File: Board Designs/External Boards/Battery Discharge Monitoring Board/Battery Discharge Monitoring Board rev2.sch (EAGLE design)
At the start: 76 parts, among them Q1 LMMBT3904LT3G, Q2 LMMBT3904LT3G, Q3 LMMBT3904LT3G, Q4 LMMBT3904LT3G

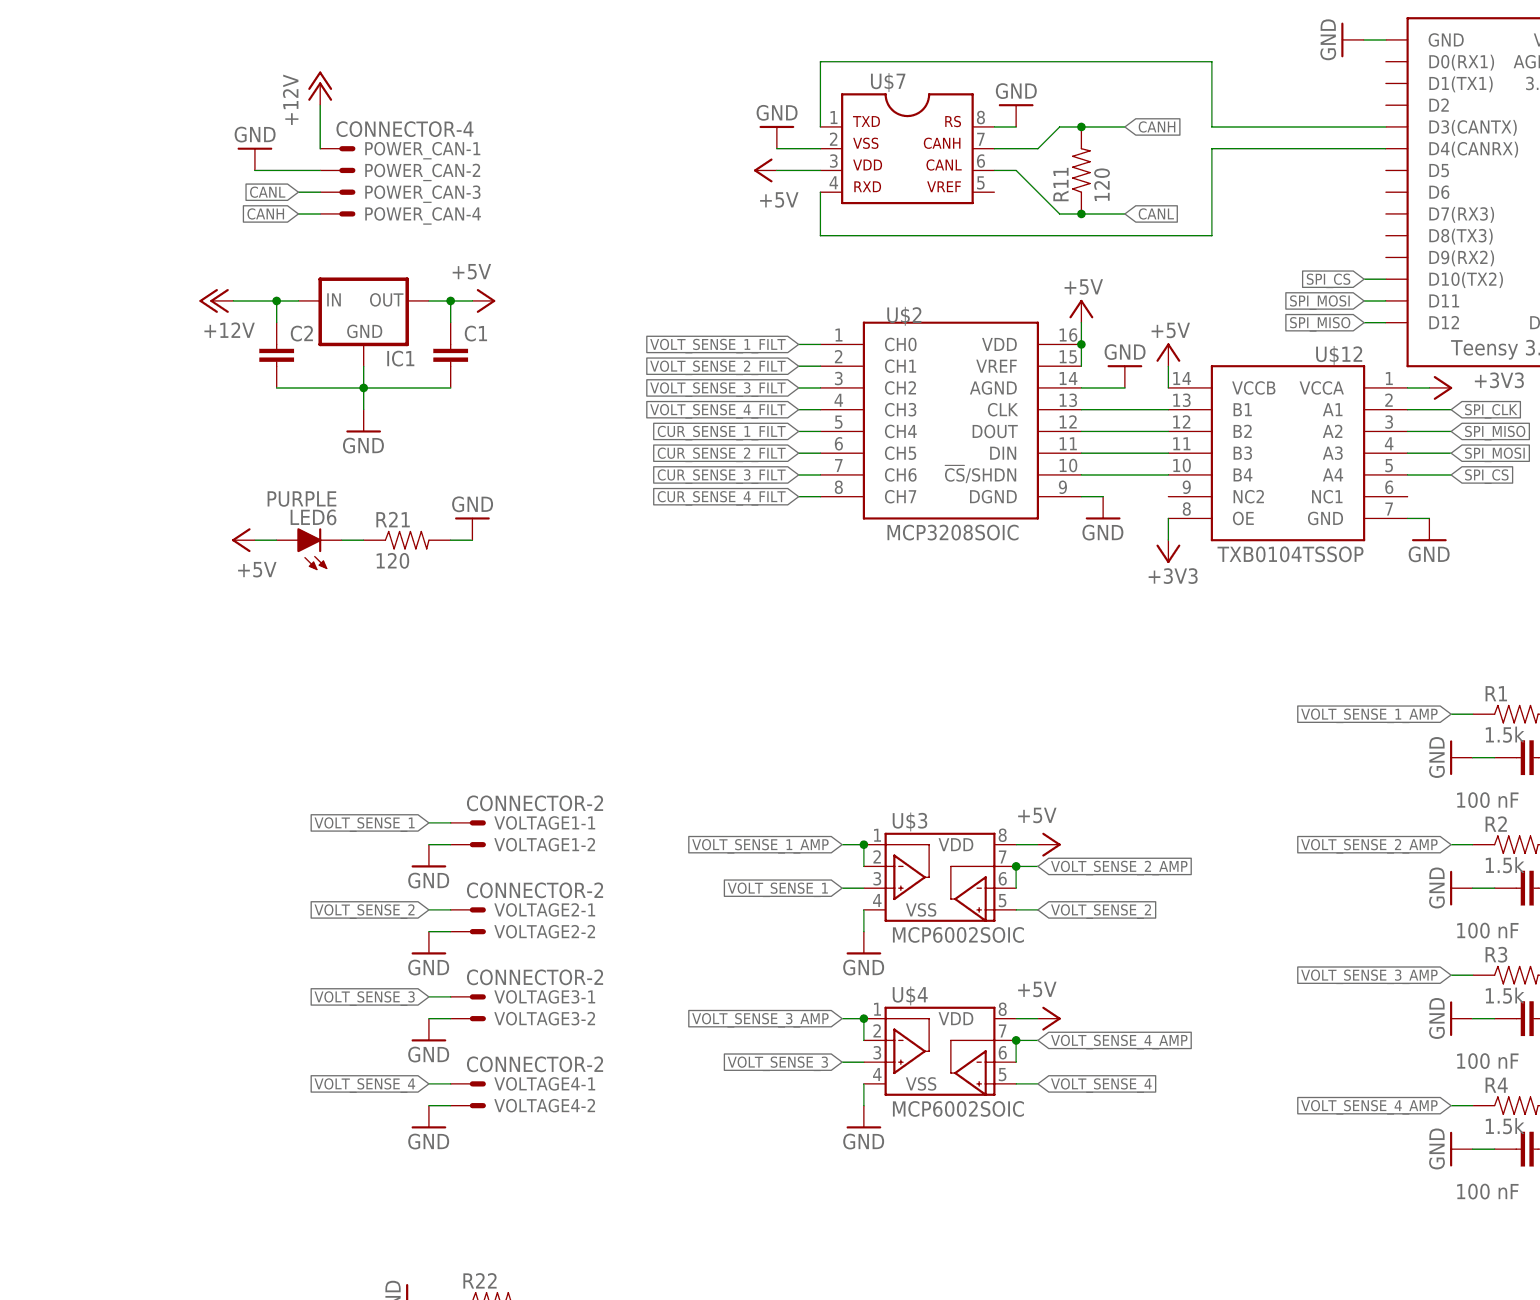
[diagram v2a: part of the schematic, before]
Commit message: Added pull down resistors and button
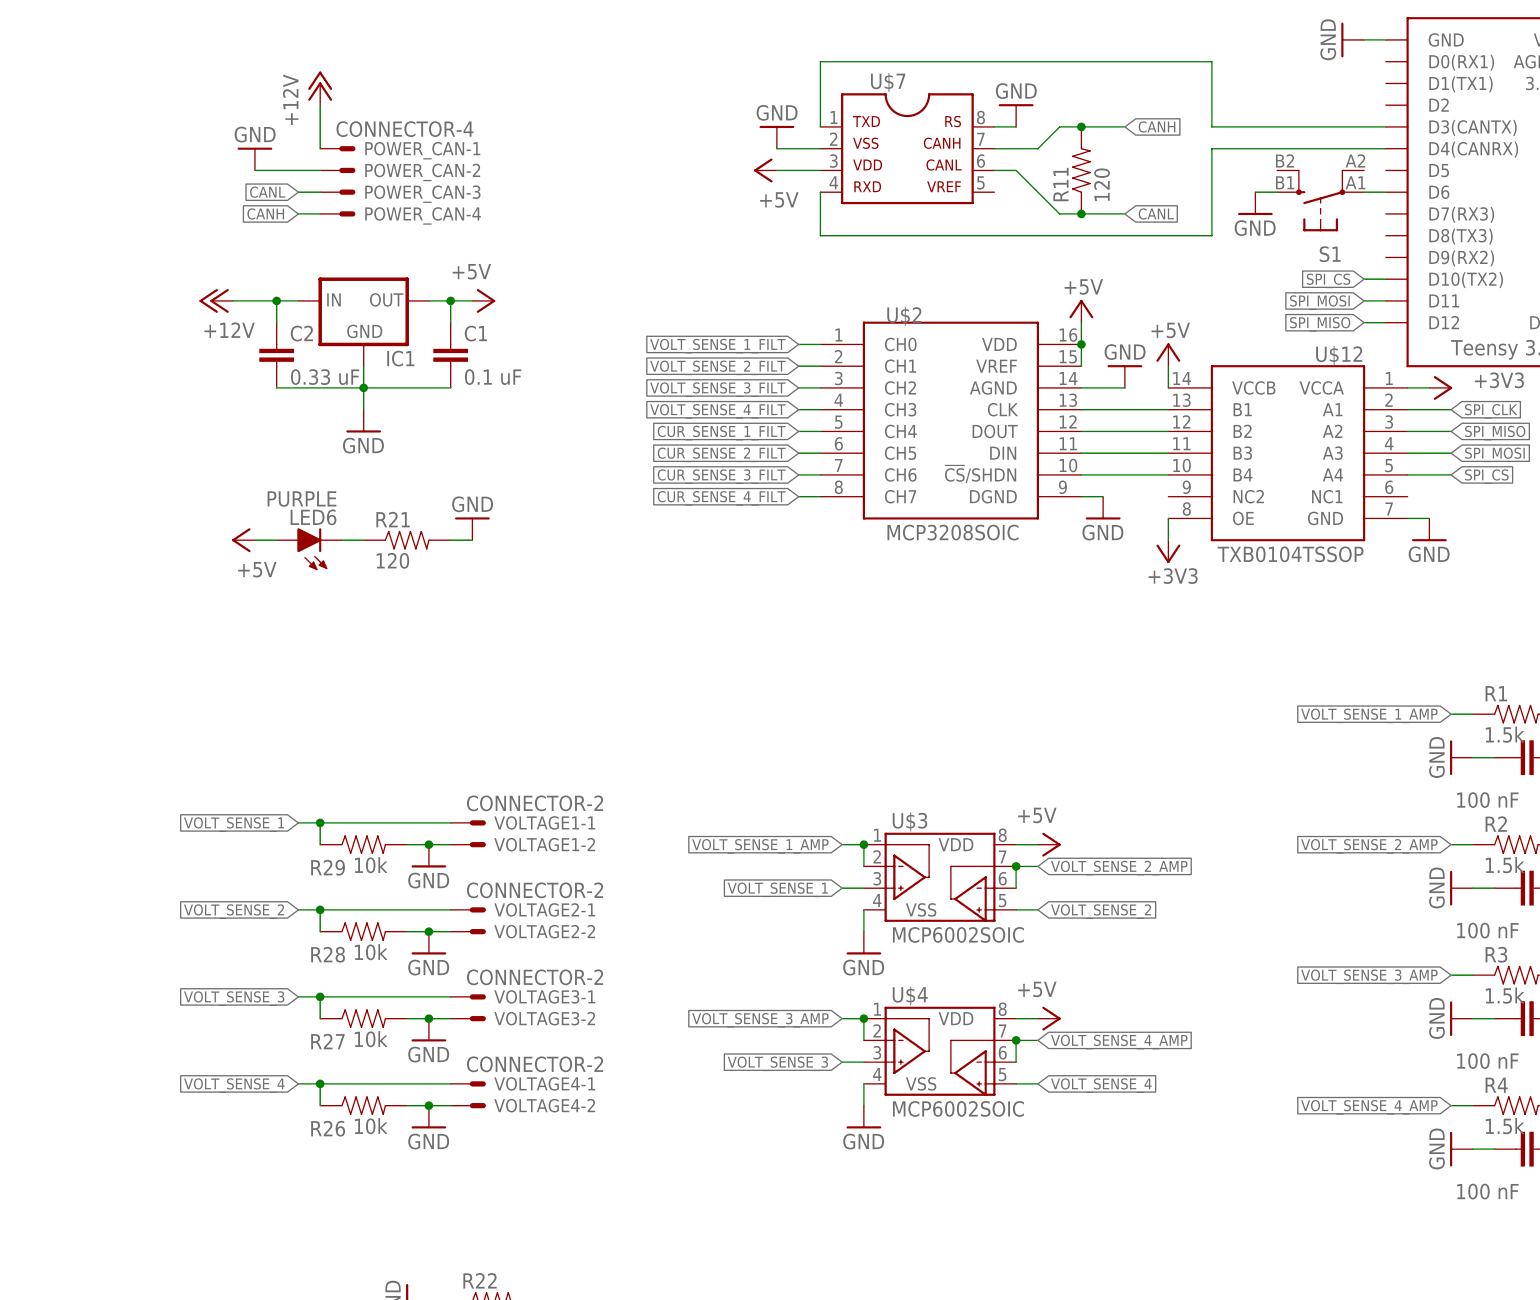
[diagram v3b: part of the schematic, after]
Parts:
- added R26, R27, R28, R29: 10k, HyTechDevices:RESISTOR0805-RES
- added S1: (no value), HyTechDevices:BTN_10-XXSMD
- C1: value (none) -> 0.1 uF
- C2: value (none) -> 0.33 uF
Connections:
- new net N$17: U$12.B1, U$2.CLK
- new net N$18: U$12.B2, U$2.DOUT
- new net N$19: U$12.B3, U$2.DIN
- new net N$20: U$12.B4, U$2.!CS!/SHDN
- new net N$21: S1.P, U$1.D6
- net GND: now also R26.2, R27.2, R28.2, R29.2, S1.S
- net SPI_CLK: no longer U$12.B1, U$2.CLK
- net SPI_CS: no longer U$12.B4, U$2.!CS!/SHDN
- net SPI_MISO: no longer U$12.B2, U$2.DOUT
- net SPI_MOSI: no longer U$12.B3, U$2.DIN
- net VOLT_SENSE_1: now also R29.1
- net VOLT_SENSE_2: now also R28.1
- net VOLT_SENSE_3: now also R27.1
- net VOLT_SENSE_4: now also R26.1
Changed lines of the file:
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@@
 <?xml version="1.0" encoding="utf-8"?>
 <!DOCTYPE eagle SYSTEM "eagle.dtd">
-<eagle version="9.2.2">
+<eagle version="9.3.0">
 <drawing>
 <settings>
@@
 <part name="P+6" library="supply1" library_urn="urn:adsk.eagle:library:371" deviceset="+5V" device=""/>
 <part name="GND11" library="supply1" library_urn="urn:adsk.eagle:library:371" deviceset="GND" device=""/>
-<part name="C1" library="HyTechDevices" deviceset="CAP" device="0805"/>
-<part name="C2" library="HyTechDevices" deviceset="CAP" device="0805"/>
+<part name="C1" library="HyTechDevices" deviceset="CAP" device="0805" value="0.1 uF"/>
+<part name="C2" library="HyTechDevices" deviceset="CAP" device="0805" value="0.33 uF"/>
 <part name="P+7" library="supply1" library_urn="urn:adsk.eagle:library:371" deviceset="+12V" device=""/>
 <part name="C3" library="HyTechDevices" deviceset="CAP" device="0805" value="100 nF"/>
@@
 <part name="GND52" library="supply1" library_urn="urn:adsk.eagle:library:371" deviceset="GND" device=""/>
 <part name="P+24" library="supply1" library_urn="urn:adsk.eagle:library:371" deviceset="+5V" device=""/>
+<part name="R26" library="HyTechDevices" deviceset="RESISTOR" device="0805-RES" value="10k"/>
+<part name="R27" library="HyTechDevices" deviceset="RESISTOR" device="0805-RES" value="10k"/>
+<part name="R28" library="HyTechDevices" deviceset="RESISTOR" device="0805-RES" value="10k"/>
+<part name="R29" library="HyTechDevices" deviceset="RESISTOR" device="0805-RES" value="10k"/>
+<part name="S1" library="HyTechDevices" deviceset="BTN_10-XX" device="SMD"/>
+<part name="GND53" library="supply1" library_urn="urn:adsk.eagle:library:371" deviceset="GND" device=""/>
 </parts>
 <sheets>
@@
 <attribute name="VALUE" x="119.38" y="185.42" size="1.778" layer="96" rot="R180"/>
 </instance>
+<instance part="R26" gate="G$1" x="22.86" y="93.98" smashed="yes">
+<attribute name="NAME" x="16.51" y="90.3986" size="1.778" layer="95"/>
+<attribute name="VALUE" x="21.59" y="90.678" size="1.778" layer="96"/>
+</instance>
+<instance part="R27" gate="G$1" x="22.86" y="104.14" smashed="yes">
+<attribute name="NAME" x="16.51" y="100.5586" size="1.778" layer="95"/>
+<attribute name="VALUE" x="21.59" y="100.838" size="1.778" layer="96"/>
+</instance>
+<instance part="R28" gate="G$1" x="22.86" y="114.3" smashed="yes">
+<attribute name="NAME" x="16.51" y="110.7186" size="1.778" layer="95"/>
+<attribute name="VALUE" x="21.59" y="110.998" size="1.778" layer="96"/>
+</instance>
+<instance part="R29" gate="G$1" x="22.86" y="124.46" smashed="yes">
+<attribute name="NAME" x="16.51" y="120.8786" size="1.778" layer="95"/>
+<attribute name="VALUE" x="21.59" y="121.158" size="1.778" layer="96"/>
+</instance>
+<instance part="S1" gate="1" x="134.62" y="200.66" smashed="yes" rot="R90">
+<attribute name="NAME" x="137.16" y="194.31" size="1.778" layer="95" rot="R180"/>
+<attribute name="VALUE" x="131.445" y="196.85" size="1.778" layer="96" rot="R180"/>
+</instance>
+<instance part="GND53" gate="1" x="127" y="198.12" smashed="yes">
+<attribute name="VALUE" x="124.46" y="195.58" size="1.778" layer="96"/>
+</instance>
 </instances>
 <busses>
@@
 <pinref part="GND5" gate="1" pin="GND"/>
 <wire x1="30.48" y1="124.46" x2="33.02" y2="124.46" width="0.1524" layer="91"/>
+<pinref part="R29" gate="G$1" pin="2"/>
+<wire x1="27.94" y1="124.46" x2="30.48" y2="124.46" width="0.1524" layer="91"/>
+<junction x="30.48" y="124.46"/>
 </segment>
 <segment>
@@
 <pinref part="GND6" gate="1" pin="GND"/>
 <wire x1="30.48" y1="114.3" x2="33.02" y2="114.3" width="0.1524" layer="91"/>
+<pinref part="R28" gate="G$1" pin="2"/>
+<wire x1="27.94" y1="114.3" x2="30.48" y2="114.3" width="0.1524" layer="91"/>
+<junction x="30.48" y="114.3"/>
 </segment>
 <segment>
@@
 <pinref part="GND7" gate="1" pin="GND"/>
 <wire x1="30.48" y1="104.14" x2="33.02" y2="104.14" width="0.1524" layer="91"/>
+<pinref part="R27" gate="G$1" pin="2"/>
+<wire x1="27.94" y1="104.14" x2="30.48" y2="104.14" width="0.1524" layer="91"/>
+<junction x="30.48" y="104.14"/>
 </segment>
 <segment>
@@
 <pinref part="GND8" gate="1" pin="GND"/>
 <wire x1="30.48" y1="93.98" x2="33.02" y2="93.98" width="0.1524" layer="91"/>
+<pinref part="R26" gate="G$1" pin="2"/>
+<wire x1="27.94" y1="93.98" x2="30.48" y2="93.98" width="0.1524" layer="91"/>
+<junction x="30.48" y="93.98"/>
 </segment>
 <segment>
@@
 <pinref part="U$12" gate="G$1" pin="GND"/>
 </segment>
+<segment>
+<pinref part="GND53" gate="1" pin="GND"/>
+<wire x1="127" y1="200.66" x2="129.54" y2="200.66" width="0.1524" layer="91"/>
+<pinref part="S1" gate="1" pin="S"/>
+</segment>
 </net>
 <net name="CUR_SENSE_1" class="0">
@@
 <segment>
 <pinref part="VOLTAGE1" gate="-1" pin="S"/>
-<wire x1="33.02" y1="127" x2="30.48" y2="127" width="0.1524" layer="91"/>
-<label x="30.48" y="127" size="1.27" layer="95" rot="R180" xref="yes"/>
+<wire x1="33.02" y1="127" x2="17.78" y2="127" width="0.1524" layer="91"/>
+<label x="15.24" y="127" size="1.27" layer="95" rot="R180" xref="yes"/>
+<pinref part="R29" gate="G$1" pin="1"/>
+<wire x1="17.78" y1="127" x2="15.24" y2="127" width="0.1524" layer="91"/>
+<wire x1="17.78" y1="124.46" x2="17.78" y2="127" width="0.1524" layer="91"/>
+<junction x="17.78" y="127"/>
 </segment>
 <segment>
@@
 <segment>
 <pinref part="VOLTAGE2" gate="-1" pin="S"/>
-<wire x1="33.02" y1="116.84" x2="30.48" y2="116.84" width="0.1524" layer="91"/>
-<label x="30.48" y="116.84" size="1.27" layer="95" rot="R180" xref="yes"/>
+<wire x1="33.02" y1="116.84" x2="17.78" y2="116.84" width="0.1524" layer="91"/>
+<label x="15.24" y="116.84" size="1.27" layer="95" rot="R180" xref="yes"/>
+<pinref part="R28" gate="G$1" pin="1"/>
+<wire x1="17.78" y1="116.84" x2="15.24" y2="116.84" width="0.1524" layer="91"/>
+<wire x1="17.78" y1="114.3" x2="17.78" y2="116.84" width="0.1524" layer="91"/>
+<junction x="17.78" y="116.84"/>
 </segment>
 <segment>
@@
 <segment>
 <pinref part="VOLTAGE3" gate="-1" pin="S"/>
-<wire x1="33.02" y1="106.68" x2="30.48" y2="106.68" width="0.1524" layer="91"/>
-<label x="30.48" y="106.68" size="1.27" layer="95" rot="R180" xref="yes"/>
+<wire x1="33.02" y1="106.68" x2="17.78" y2="106.68" width="0.1524" layer="91"/>
+<label x="15.24" y="106.68" size="1.27" layer="95" rot="R180" xref="yes"/>
+<pinref part="R27" gate="G$1" pin="1"/>
+<wire x1="17.78" y1="106.68" x2="15.24" y2="106.68" width="0.1524" layer="91"/>
+<wire x1="17.78" y1="104.14" x2="17.78" y2="106.68" width="0.1524" layer="91"/>
+<junction x="17.78" y="106.68"/>
 </segment>
 <segment>
@@
 <segment>
 <pinref part="VOLTAGE4" gate="-1" pin="S"/>
-<wire x1="33.02" y1="96.52" x2="30.48" y2="96.52" width="0.1524" layer="91"/>
-<label x="30.48" y="96.52" size="1.27" layer="95" rot="R180" xref="yes"/>
+<wire x1="33.02" y1="96.52" x2="17.78" y2="96.52" width="0.1524" layer="91"/>
+<label x="15.24" y="96.52" size="1.27" layer="95" rot="R180" xref="yes"/>
+<pinref part="R26" gate="G$1" pin="1"/>
+<wire x1="17.78" y1="96.52" x2="15.24" y2="96.52" width="0.1524" layer="91"/>
+<wire x1="17.78" y1="96.52" x2="17.78" y2="93.98" width="0.1524" layer="91"/>
+<junction x="17.78" y="96.52"/>
 </segment>
 <segment>
@@
 <net name="SPI_CLK" class="0">
 <segment>
-<pinref part="U$2" gate="G$1" pin="CLK"/>
-<pinref part="U$12" gate="G$1" pin="B1"/>
-<wire x1="116.84" y1="175.26" x2="106.68" y2="175.26" width="0.1524" layer="91"/>
-</segment>
-<segment>
 <pinref part="U$1" gate="G$1" pin="D13"/>
 <wire x1="170.18" y1="185.42" x2="167.64" y2="185.42" width="0.1524" layer="91"/>
@@
 <net name="SPI_MISO" class="0">
 <segment>
-<pinref part="U$2" gate="G$1" pin="DOUT"/>
-<pinref part="U$12" gate="G$1" pin="B2"/>
-<wire x1="116.84" y1="172.72" x2="106.68" y2="172.72" width="0.1524" layer="91"/>
-</segment>
-<segment>
 <pinref part="U$1" gate="G$1" pin="D12"/>
 <wire x1="142.24" y1="185.42" x2="139.7" y2="185.42" width="0.1524" layer="91"/>
@@
 <net name="SPI_MOSI" class="0">
 <segment>
-<pinref part="U$2" gate="G$1" pin="DIN"/>
-<pinref part="U$12" gate="G$1" pin="B3"/>
-<wire x1="106.68" y1="170.18" x2="116.84" y2="170.18" width="0.1524" layer="91"/>
-</segment>
-<segment>
 <pinref part="U$1" gate="G$1" pin="D11"/>
 <wire x1="142.24" y1="187.96" x2="139.7" y2="187.96" width="0.1524" layer="91"/>
@@
 </net>
 <net name="SPI_CS" class="0">
-<segment>
-<pinref part="U$2" gate="G$1" pin="!CS!/SHDN"/>
-<pinref part="U$12" gate="G$1" pin="B4"/>
-<wire x1="116.84" y1="167.64" x2="106.68" y2="167.64" width="0.1524" layer="91"/>
-</segment>
 <segment>
 <pinref part="U$1" gate="G$1" pin="D10(TX2)"/>
@@
 </segment>
 </net>
+<net name="N$17" class="0">
+<segment>
+<pinref part="U$2" gate="G$1" pin="CLK"/>
+<pinref part="U$12" gate="G$1" pin="B1"/>
+<wire x1="106.68" y1="175.26" x2="116.84" y2="175.26" width="0.1524" layer="91"/>
+</segment>
+</net>
+<net name="N$18" class="0">
+<segment>
+<pinref part="U$12" gate="G$1" pin="B2"/>
+<pinref part="U$2" gate="G$1" pin="DOUT"/>
+<wire x1="116.84" y1="172.72" x2="106.68" y2="172.72" width="0.1524" layer="91"/>
+</segment>
+</net>
+<net name="N$19" class="0">
+<segment>
+<pinref part="U$2" gate="G$1" pin="DIN"/>
+<pinref part="U$12" gate="G$1" pin="B3"/>
+<wire x1="106.68" y1="170.18" x2="116.84" y2="170.18" width="0.1524" layer="91"/>
+</segment>
+</net>
+<net name="N$20" class="0">
+<segment>
+<pinref part="U$12" gate="G$1" pin="B4"/>
+<pinref part="U$2" gate="G$1" pin="!CS!/SHDN"/>
+<wire x1="116.84" y1="167.64" x2="106.68" y2="167.64" width="0.1524" layer="91"/>
+</segment>
+</net>
+<net name="N$21" class="0">
+<segment>
+<pinref part="S1" gate="1" pin="P"/>
+<pinref part="U$1" gate="G$1" pin="D6"/>
+<wire x1="139.7" y1="200.66" x2="142.24" y2="200.66" width="0.1524" layer="91"/>
+</segment>
+</net>
